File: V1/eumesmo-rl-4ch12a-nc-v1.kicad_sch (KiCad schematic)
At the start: 24 parts, among them J1 250-202, J2 250-204, J3 DB142V-5.08-4P, J4 DB142V-5.08-4P, K1 Songle_SRD_1B, K2 Songle_SRD_1B, K3 Songle_SRD_1B, K4 Songle_SRD_1B

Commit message: LEDs changed to orange
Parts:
- D1, D3, D5, D7: value GREEN -> ORANGE/0603; LCSC Part # C72043 -> C2987557; Mfr Everlight -> Everlight Elec; Mfr PN 19-217/GHC-YR1S2/3T -> 19-217/S2C-AL1M2VY/6T; Vendor PN C72043 -> C2987557
- R1, R2, R3, R4: value 10k/125mW -> 9.1k/125mW; LCSC Part # C17414 -> C17855; Mfr PN 0805W8F1002T5E -> 0805W8F9101T5E; Vendor PN C17414 -> C17855
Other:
- note added: "V_{F} = 1,8V @ 2,5mA I_{LED} = (24V - V_{F}) / R I_{LED} = (24V - 1.8V) / 9.1k I_{LED} = 2.44 mA"
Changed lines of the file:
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@@
 		(rev "V1.2")
 	)
-	(junction
-		(at 68.58 144.78)
-		(diameter 0)
-		(color 0 0 0 0)
+	(text "V_{F} = 1,8V @ 2,5mA\nI_{LED} = (24V - V_{F}) / R\nI_{LED} = (24V - 1.8V) / 9.1k\nI_{LED} = 2.44 mA"
+		(exclude_from_sim no)
+		(at 63.5 161.29 0)
+		(effects
+			(font
+				(size 1.5 1.5)
+			)
+			(justify left bottom)
+		)
 	)
 	(junction
@@
 	)
 	(junction
-		(at 162.56 147.32)
-		(diameter 0)
-		(color 0 0 0 0)
-	)
-	(junction
 		(at 171.45 147.32)
 		(diameter 0)
@@
 	)
 	(junction
+		(at 162.56 147.32)
+		(diameter 0)
+		(color 0 0 0 0)
+	)
+	(junction
 		(at 68.58 93.98)
 		(diameter 0)
 		(color 0 0 0 0)
 	)
+	(junction
+		(at 68.58 144.78)
+		(diameter 0)
+		(color 0 0 0 0)
+	)
 	(wire
 		(pts
@@
 	(wire
 		(pts
-			(xy 53.34 144.78) (xy 68.58 144.78)
+			(xy 48.26 144.78) (xy 68.58 144.78)
 		)
 		(stroke
@@
 	(wire
 		(pts
-			(xy 53.34 144.78) (xy 53.34 99.06)
+			(xy 48.26 144.78) (xy 48.26 99.06)
 		)
 		(stroke
@@
 	(wire
 		(pts
-			(xy 50.8 147.32) (xy 162.56 147.32)
+			(xy 45.72 147.32) (xy 162.56 147.32)
 		)
 		(stroke
@@
 	(wire
 		(pts
-			(xy 53.34 99.06) (xy 33.02 99.06)
+			(xy 48.26 99.06) (xy 33.02 99.06)
 		)
 		(stroke
@@
 	(wire
 		(pts
-			(xy 50.8 101.6) (xy 33.02 101.6)
+			(xy 45.72 101.6) (xy 33.02 101.6)
 		)
 		(stroke
@@
 	(wire
 		(pts
-			(xy 50.8 147.32) (xy 50.8 101.6)
+			(xy 45.72 147.32) (xy 45.72 101.6)
 		)
 		(stroke
@@
 			)
 		)
-		(property "Value" "GREEN"
+		(property "Value" "ORANGE/0603"
 			(at 160.02 140.97 90)
 			(show_name no)
@@
 			)
 		)
-		(property "Mfr" "Everlight"
+		(property "Mfr" "Everlight Elec"
 			(at 162.56 140.97 0)
 			(hide yes)
@@
 			)
 		)
-		(property "Mfr PN" "19-217/GHC-YR1S2/3T"
+		(property "Mfr PN" "19-217/S2C-AL1M2VY/6T"
 			(at 162.56 140.97 0)
 			(hide yes)
@@
 			)
 		)
-		(property "Vendor PN" "C72043"
+		(property "Vendor PN" "C2987557"
 			(at 162.56 140.97 0)
 			(hide yes)
@@
 			)
 		)
-		(property "LCSC Part #" "C72043"
+		(property "LCSC Part #" "C2987557"
 			(at 160.02 143.51 90)
 			(show_name no)
@@
 			)
 		)
-		(property "Value" "10k/125mW"
+		(property "Value" "9.1k/125mW"
 			(at 66.04 71.12 0)
 			(show_name no)
@@
 			)
 		)
-		(property "Mfr PN" "0805W8F1002T5E"
+		(property "Mfr PN" "0805W8F9101T5E"
 			(at 68.58 71.12 0)
 			(hide yes)
@@
 			)
 		)
-		(property "Vendor PN" "C17414"
+		(property "Vendor PN" "C17855"
 			(at 68.58 71.12 0)
 			(hide yes)
@@
 			)
 		)
-		(property "LCSC Part #" "C17414"
+		(property "LCSC Part #" "C17855"
 			(at 66.04 73.66 0)
 			(show_name no)
@@
 			)
 		)
-		(property "Value" "GREEN"
+		(property "Value" "ORANGE/0603"
 			(at 66.04 138.43 90)
 			(show_name no)
@@
 			)
 		)
-		(property "Mfr" "Everlight"
+		(property "Mfr" "Everlight Elec"
 			(at 68.58 138.43 0)
 			(hide yes)
@@
 			)
 		)
-		(property "Mfr PN" "19-217/GHC-YR1S2/3T"
+		(property "Mfr PN" "19-217/S2C-AL1M2VY/6T"
 			(at 68.58 138.43 0)
 			(hide yes)
@@
 			)
 		)
-		(property "Vendor PN" "C72043"
+		(property "Vendor PN" "C2987557"
 			(at 68.58 138.43 0)
 			(hide yes)
@@
 			)
 		)
-		(property "LCSC Part #" "C72043"
+		(property "LCSC Part #" "C2987557"
 			(at 66.04 140.97 90)
 			(show_name no)
@@
 			)
 		)
-		(property "Value" "10k/125mW"
+		(property "Value" "9.1k/125mW"
 			(at 66.04 121.92 0)
 			(show_name no)
@@
 			)
 		)
-		(property "Mfr PN" "0805W8F1002T5E"
+		(property "Mfr PN" "0805W8F9101T5E"
 			(at 68.58 121.92 0)
 			(hide yes)
@@
 			)
 		)
-		(property "Vendor PN" "C17414"
+		(property "Vendor PN" "C17855"
 			(at 68.58 121.92 0)
 			(hide yes)
@@
 			)
 		)
-		(property "LCSC Part #" "C17414"
+		(property "LCSC Part #" "C17855"
 			(at 66.04 124.46 0)
 			(show_name no)
@@
 			)
 		)
-		(property "Value" "10k/125mW"
+		(property "Value" "9.1k/125mW"
 			(at 160.02 125.73 0)
 			(show_name no)
@@
 			)
 		)
-		(property "Mfr PN" "0805W8F1002T5E"
+		(property "Mfr PN" "0805W8F9101T5E"
 			(at 162.56 125.73 0)
 			(hide yes)
@@
 			)
 		)
-		(property "Vendor PN" "C17414"
+		(property "Vendor PN" "C17855"
 			(at 162.56 125.73 0)
 			(hide yes)
@@
 			)
 		)
-		(property "LCSC Part #" "C17414"
+		(property "LCSC Part #" "C17855"
 			(at 160.02 128.27 0)
 			(show_name no)
@@
 			)
 		)
-		(property "Value" "GREEN"
+		(property "Value" "ORANGE/0603"
 			(at 66.04 87.63 90)
 			(show_name no)
@@
 			)
 		)
-		(property "Mfr" "Everlight"
+		(property "Mfr" "Everlight Elec"
 			(at 68.58 87.63 0)
 			(hide yes)
@@
 			)
 		)
-		(property "Mfr PN" "19-217/GHC-YR1S2/3T"
+		(property "Mfr PN" "19-217/S2C-AL1M2VY/6T"
 			(at 68.58 87.63 0)
 			(hide yes)
@@
 			)
 		)
-		(property "Vendor PN" "C72043"
+		(property "Vendor PN" "C2987557"
 			(at 68.58 87.63 0)
 			(hide yes)
@@
 			)
 		)
-		(property "LCSC Part #" "C72043"
+		(property "LCSC Part #" "C2987557"
 			(at 66.04 90.17 90)
 			(show_name no)
@@
 			)
 		)
-		(property "Value" "10k/125mW"
+		(property "Value" "9.1k/125mW"
 			(at 160.02 74.93 0)
 			(show_name no)
@@
 			)
 		)
-		(property "Mfr PN" "0805W8F1002T5E"
+		(property "Mfr PN" "0805W8F9101T5E"
 			(at 162.56 74.93 0)
 			(hide yes)
@@
 			)
 		)
-		(property "Vendor PN" "C17414"
+		(property "Vendor PN" "C17855"
 			(at 162.56 74.93 0)
 			(hide yes)
@@
 			)
 		)
-		(property "LCSC Part #" "C17414"
+		(property "LCSC Part #" "C17855"
 			(at 160.02 77.47 0)
 			(show_name no)
@@
 			)
 		)
-		(property "Value" "GREEN"
+		(property "Value" "ORANGE/0603"
 			(at 160.02 90.17 90)
 			(show_name no)
@@
 			)
 		)
-		(property "Mfr" "Everlight"
+		(property "Mfr" "Everlight Elec"
 			(at 162.56 90.17 0)
 			(hide yes)
@@
 			)
 		)
-		(property "Mfr PN" "19-217/GHC-YR1S2/3T"
+		(property "Mfr PN" "19-217/S2C-AL1M2VY/6T"
 			(at 162.56 90.17 0)
 			(hide yes)
@@
 			)
 		)
-		(property "Vendor PN" "C72043"
+		(property "Vendor PN" "C2987557"
 			(at 162.56 90.17 0)
 			(hide yes)
@@
 			)
 		)
-		(property "LCSC Part #" "C72043"
+		(property "LCSC Part #" "C2987557"
 			(at 160.02 92.71 90)
 			(show_name no)

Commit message: LEDs replaced for orange
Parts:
- R1, R2, R3, R4: value 9.1k/125mW -> 10k/125mW; LCSC Part # C17855 -> C17414; Mfr PN 0805W8F9101T5E -> 0805W8F1002T5E; Vendor PN C17855 -> C17414
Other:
- note added: "V_{F} = 1,8V @ 2,5mA I_{LED} = (24V - V_{F}) / R I_{LED} = (24V - 1.8V) / 10k I_{LED} = 2.22 mA"
- note removed: "V_{F} = 1,8V @ 2,5mA I_{LED} = (24V - V_{F}) / R I_{LED} = (24V - 1.8V) / 9.1k I_{LED} = 2.44 mA"
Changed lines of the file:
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@@
 		(rev "V1.2")
 	)
-	(text "V_{F} = 1,8V @ 2,5mA\nI_{LED} = (24V - V_{F}) / R\nI_{LED} = (24V - 1.8V) / 9.1k\nI_{LED} = 2.44 mA"
+	(text "V_{F} = 1,8V @ 2,5mA\nI_{LED} = (24V - V_{F}) / R\nI_{LED} = (24V - 1.8V) / 10k\nI_{LED} = 2.22 mA"
 		(exclude_from_sim no)
 		(at 63.5 161.29 0)
@@
 			)
 		)
-		(property "Value" "9.1k/125mW"
+		(property "Value" "10k/125mW"
 			(at 66.04 71.12 0)
 			(show_name no)
@@
 			)
 		)
-		(property "Mfr PN" "0805W8F9101T5E"
+		(property "Mfr PN" "0805W8F1002T5E"
 			(at 68.58 71.12 0)
 			(hide yes)
@@
 			)
 		)
-		(property "Vendor PN" "C17855"
+		(property "Vendor PN" "C17414"
 			(at 68.58 71.12 0)
 			(hide yes)
@@
 			)
 		)
-		(property "LCSC Part #" "C17855"
+		(property "LCSC Part #" "C17414"
 			(at 66.04 73.66 0)
 			(show_name no)
@@
 			)
 		)
-		(property "Value" "9.1k/125mW"
+		(property "Value" "10k/125mW"
 			(at 66.04 121.92 0)
 			(show_name no)
@@
 			)
 		)
-		(property "Mfr PN" "0805W8F9101T5E"
+		(property "Mfr PN" "0805W8F1002T5E"
 			(at 68.58 121.92 0)
 			(hide yes)
@@
 			)
 		)
-		(property "Vendor PN" "C17855"
+		(property "Vendor PN" "C17414"
 			(at 68.58 121.92 0)
 			(hide yes)
@@
 			)
 		)
-		(property "LCSC Part #" "C17855"
+		(property "LCSC Part #" "C17414"
 			(at 66.04 124.46 0)
 			(show_name no)
@@
 			)
 		)
-		(property "Value" "9.1k/125mW"
+		(property "Value" "10k/125mW"
 			(at 160.02 125.73 0)
 			(show_name no)
@@
 			)
 		)
-		(property "Mfr PN" "0805W8F9101T5E"
+		(property "Mfr PN" "0805W8F1002T5E"
 			(at 162.56 125.73 0)
 			(hide yes)
@@
 			)
 		)
-		(property "Vendor PN" "C17855"
+		(property "Vendor PN" "C17414"
 			(at 162.56 125.73 0)
 			(hide yes)
@@
 			)
 		)
-		(property "LCSC Part #" "C17855"
+		(property "LCSC Part #" "C17414"
 			(at 160.02 128.27 0)
 			(show_name no)
@@
 			)
 		)
-		(property "Value" "9.1k/125mW"
+		(property "Value" "10k/125mW"
 			(at 160.02 74.93 0)
 			(show_name no)
@@
 			)
 		)
-		(property "Mfr PN" "0805W8F9101T5E"
+		(property "Mfr PN" "0805W8F1002T5E"
 			(at 162.56 74.93 0)
 			(hide yes)
@@
 			)
 		)
-		(property "Vendor PN" "C17855"
+		(property "Vendor PN" "C17414"
 			(at 162.56 74.93 0)
 			(hide yes)
@@
 			)
 		)
-		(property "LCSC Part #" "C17855"
+		(property "LCSC Part #" "C17414"
 			(at 160.02 77.47 0)
 			(show_name no)

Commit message: Adjusted component rotation and offset information for JLCPCB.
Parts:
- D1, D3, D5, D7: JLCPCB BOM 1 -> (none); Package 0603/1608 -> (none)
- D2, D4, D6, D8: JLCPCB BOM 1 -> (none); Package SOD-123 -> (none)
- J1, J2, K1, K2, K3, K4: JLCPCB BOM 1 -> (none)
- J3, J4: FT Rotation Offset (none) -> 180; JLCPCB BOM 1 -> (none)
- R1, R2, R3, R4: JLCPCB BOM 1 -> (none); Package 0805/2012 -> (none)
- RV1, RV2, RV3, RV4: JLCPCB BOM 1 -> (none); Package 9.5X5.08mm -> (none)

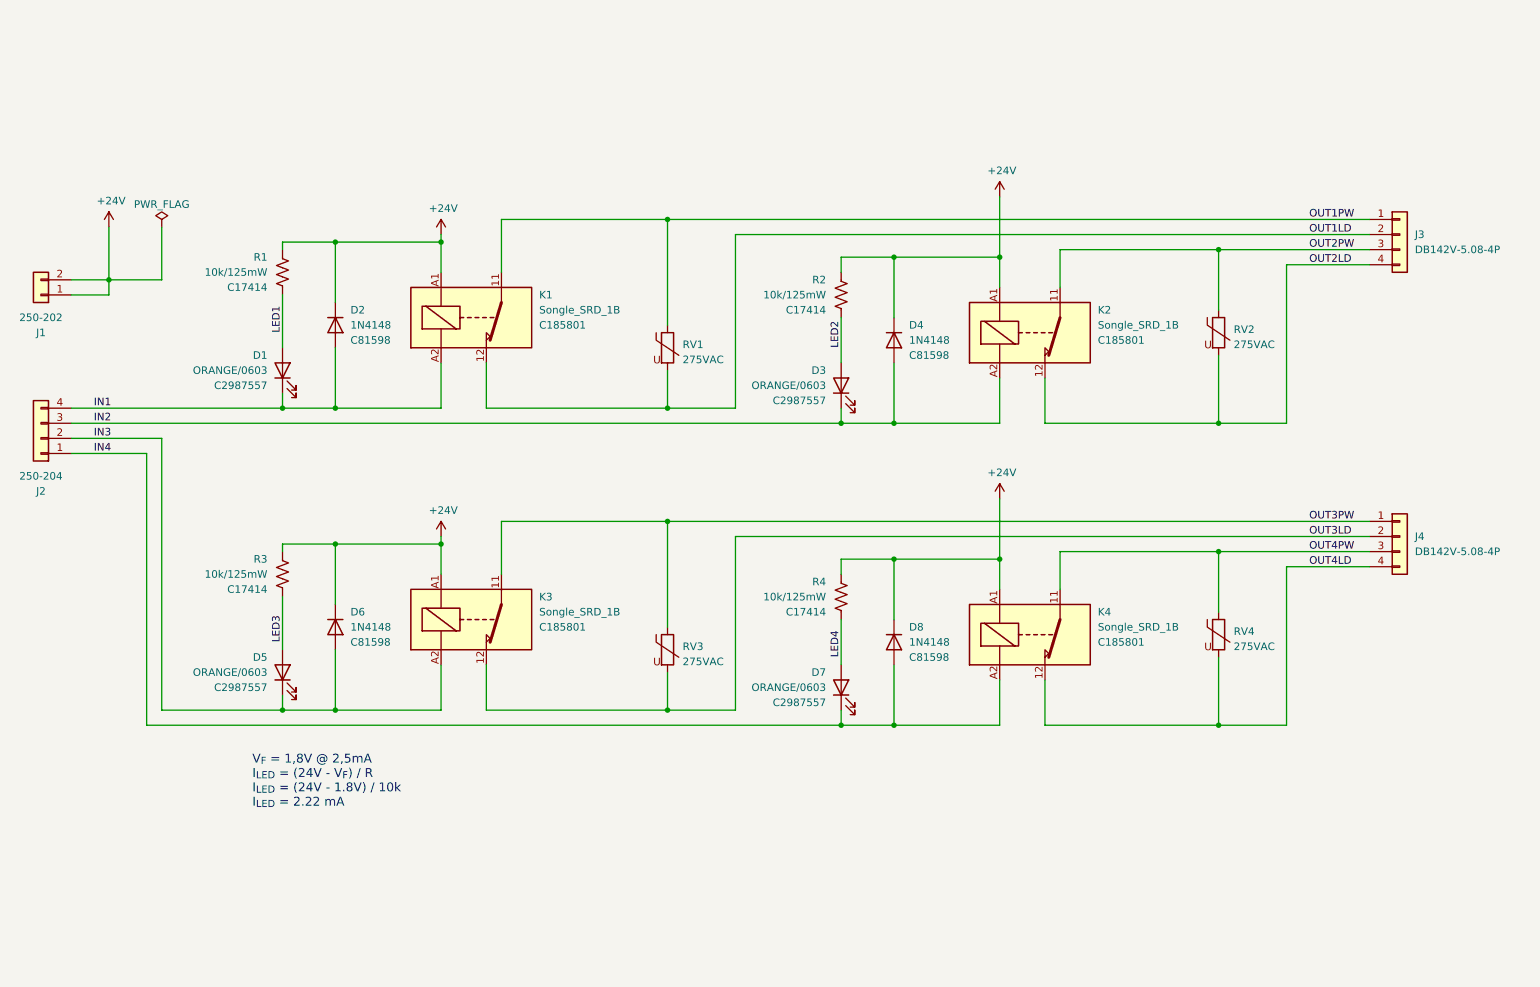
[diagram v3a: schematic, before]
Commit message: Replaced NC with form C (NO + NC) relays.
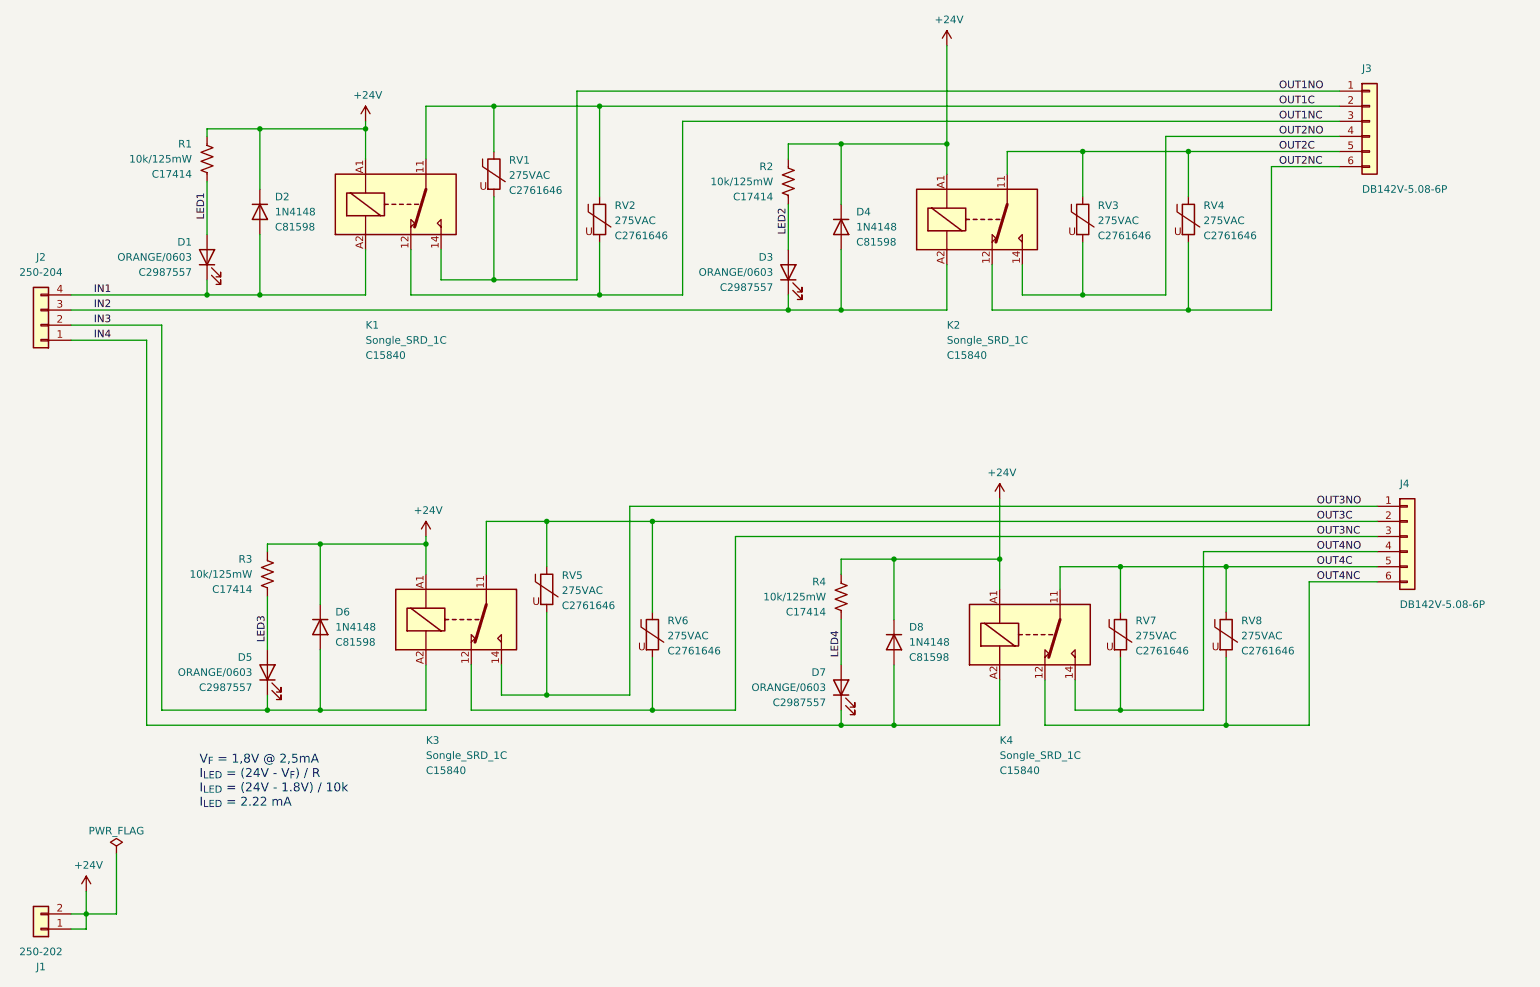
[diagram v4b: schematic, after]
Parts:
- added RV2, RV3, RV6, RV8: 275VAC, Tales:RV_Disc_D9.50mm_W3.6mm_P5.08mm, symbol Device:Varistor
- J3, J4: value DB142V-5.08-4P -> DB142V-5.08-6P; footprint Tales:TerminalBlock_Dibo_DB142V-5.08-4P_1x04_P5.08mm_Vertical -> Tales:TerminalBlock_Dibo_DB142V-5.08-6P_1x06_P5.08mm_Vertical; symbol Connector_Generic:Conn_01x04 -> Connector_Generic:Conn_01x06; LCSC Part # C2898701 -> C2898703; Mfr PN DB142V-5.08-4P-GN -> DB142V-5.08-6P-GN; Vendor PN C2898701 -> C2898703
- K1, K2, K3, K4: value Songle_SRD_1B -> Songle_SRD_1C; footprint Tales:Relay_SPST_Songle_SRD_FormB -> Tales:Relay_SPDT_Songle_SRD_FormC; symbol Tales:Songle_SRD_1B -> Tales:Songle_SRD_1C; LCSC Part # C185801 -> C15840; Mfr PN SRD-24VDC-SL-B -> SRD-24VDC-SL-C; Vendor PN C185801 -> C15840
- renumbered RV2 to RV4, RV3 to RV5, RV4 to RV7
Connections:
- removed net OUT1LD: J3.2 (Pin_2), K1.12, RV1.2
- net OUT1PW renamed OUT1C
- net OUT1C: now also J3.2 (Pin_2), RV2.1; no longer J3.1 (Pin_1)
- net OUT2LD renamed OUT2NC
- net OUT2NC: now also J3.6 (Pin_6); no longer J3.4 (Pin_4)
- net OUT2PW renamed OUT2C
- net OUT2C: now also J3.5 (Pin_5), RV3.1; no longer J3.3 (Pin_3)
- removed net OUT3LD: J4.2 (Pin_2), K3.12, RV5.2
- net OUT3PW renamed OUT3C
- net OUT3C: now also J4.2 (Pin_2), RV6.1; no longer J4.1 (Pin_1)
- net OUT4LD renamed OUT4NO
- net OUT4NO: now also K4.14; no longer K4.12
- net OUT4PW renamed OUT4C
- net OUT4C: now also J4.5 (Pin_5), RV8.1; no longer J4.3 (Pin_3)
- new net OUT1NC: J3.3 (Pin_3), K1.12, RV2.2
- new net OUT1NO: J3.1 (Pin_1), K1.14, RV1.2
- new net OUT2NO: J3.4 (Pin_4), K2.14, RV3.2
- new net OUT3NC: J4.3 (Pin_3), K3.12, RV6.2
- new net OUT3NO: J4.1 (Pin_1), K3.14, RV5.2
- new net OUT4NC: J4.6 (Pin_6), K4.12, RV8.2
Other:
- moved on the sheet: D1, D2, D3, D4, D5, D6, J1, J2, R1, R2, R3, RV1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
